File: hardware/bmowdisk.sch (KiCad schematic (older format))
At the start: 22 parts, among them CON1 IDC20, CON2 FL40YA-V36P-2X20-LF, CON3 FL40YA-V36P-2X20-LF, U1 SN74LVC8T245PW, U2 SN74LVC8T245PW, U3 SN74LVC8T245PW, U4 SN74LVC8T245PW

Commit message: Remove silk screen from 0.5" headers
Add text for connections to FPGA board

Signed-off-by: Rangel Ivanov <rangelivanov88@gmail.com>
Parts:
- CON1: value IDC20 -> TO DISK DRIVE
- CON2, CON3: value FL40YA-V36P-2X20-LF -> TO FPGA EXT3 CONN
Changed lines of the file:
@@
-$EndComp
-$Comp
-L bmowdisk-eagle-import:IDC20 CON1
-U 1 1 98085B15
-P 10450 1000
-F 0 "CON1" H 10350 1550 59  0000 L BNN
-F 1 "IDC20" H 10350 300 59  0000 L BNN
-F 2 "bmowdisk:IDC20" H 10450 1000 50  0001 C CNN
-F 3 "" H 10450 1000 50  0001 C CNN
-	1    10450 1000
-	1    0    0    -1
 $EndComp
 $Comp
@@
 	1    9850 500
 	1    0    0    -1
-$EndComp
-$Comp
-L ice40-shield-lib:FL40YA-V36P-2X20-LF CON2
-U 1 1 602FCDEE
-P 2450 2950
-F 0 "CON2" H 2450 1685 50  0000 C CNN
-F 1 "FL40YA-V36P-2X20-LF" H 2450 1776 50  0000 C CNN
-F 2 "lime2-ice40-shield:YA-V36P-2X20-LF" H 2450 1600 50  0000 C CNN
-F 3 "" H 2450 2950 60  0000 C CNN
-	1    2450 2950
-	1    0    0    1
 $EndComp
 Wire Wire Line
@@
 Text Label 2850 5800 0    48   ~ 0
 SEL
-$Comp
-L ice40-shield-lib:FL40YA-V36P-2X20-LF CON3
-U 1 1 610F6C3A
-P 2450 5900
-F 0 "CON3" H 2450 4635 50  0000 C CNN
-F 1 "FL40YA-V36P-2X20-LF" H 2450 4726 50  0000 C CNN
-F 2 "lime2-ice40-shield:YA-V36P-2X20-LF" H 2500 4500 50  0000 C CNN
-F 3 "" H 2450 5900 60  0000 C CNN
-	1    2450 5900
-	1    0    0    1
-$EndComp
 Text Label 2850 5900 0    48   ~ 0
 ~ENABLE1
@@
 NoConn ~ 2800 5100
 NoConn ~ 2800 5200
+$Comp
+L bmowdisk-eagle-import:IDC20 CON1
+U 1 1 98085B15
+P 10450 1000
+F 0 "CON1" H 10350 1550 59  0000 L BNN
+F 1 "TO DISK DRIVE" H 10200 300 59  0000 L BNN
+F 2 "bmowdisk:IDC20" H 10450 1000 50  0001 C CNN
+F 3 "" H 10450 1000 50  0001 C CNN
+	1    10450 1000
+	1    0    0    -1
+$EndComp
+$Comp
+L ice40-shield-lib:FL40YA-V36P-2X20-LF CON3
+U 1 1 610F6C3A
+P 2450 5900
+F 0 "CON3" H 2450 4635 50  0000 C CNN
+F 1 "TO FPGA EXT3 CONN" H 2450 4726 50  0000 C CNN
+F 2 "lime2-ice40-shield:YA-V36P-2X20-LF" H 2500 4500 50  0000 C CNN
+F 3 "" H 2450 5900 60  0000 C CNN
+	1    2450 5900
+	1    0    0    1
+$EndComp
+$Comp
+L ice40-shield-lib:FL40YA-V36P-2X20-LF CON2
+U 1 1 602FCDEE
+P 2450 2950
+F 0 "CON2" H 2450 1685 50  0000 C CNN
+F 1 "TO FPGA EXT3 CONN" H 2450 1776 50  0000 C CNN
+F 2 "lime2-ice40-shield:YA-V36P-2X20-LF" H 2450 1600 50  0000 C CNN
+F 3 "" H 2450 2950 60  0000 C CNN
+	1    2450 2950
+	1    0    0    1
+$EndComp
 $EndSCHEMATC

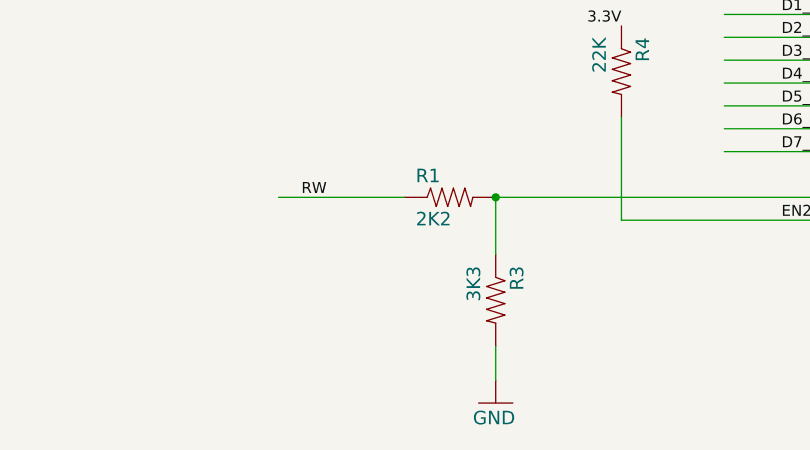
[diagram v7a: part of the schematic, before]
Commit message: Remove voltage divider for RW line to bus transceiver
Signed-off-by: Rangel Ivanov <rangelivanov88@gmail.com>
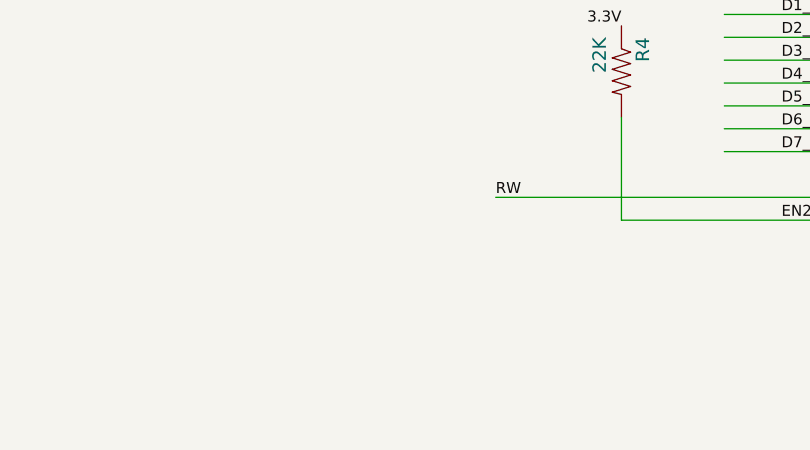
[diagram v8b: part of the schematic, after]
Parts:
- removed R1: 2K2, bmowdisk:R_0805_2012Metric_Pad1.20x1.40mm_HandSolder, symbol bmowdisk-eagle-import:RESISTOR0805-RES
- removed R3: 3K3, bmowdisk:R_0805_2012Metric_Pad1.20x1.40mm_HandSolder, symbol bmowdisk-eagle-import:RESISTOR0805-RES
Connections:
- wire segments 218 -> 215
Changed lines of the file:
@@
 Text Label 6000 9500 0    48   ~ 0
 EN245
-Text Label 3900 9400 0    48   ~ 0
+Text Label 4750 9400 0    48   ~ 0
 RW
-$Comp
-L bmowdisk-eagle-import:RESISTOR0805-RES R1
-U 1 1 62D0D96F
-P 4550 9400
-F 0 "R1" H 4400 9459 59  0000 L BNN
-F 1 "2K2" H 4400 9270 59  0000 L BNN
-F 2 "bmowdisk:R_0805_2012Metric_Pad1.20x1.40mm_HandSolder" H 4550 9400 50  0001 C CNN
-F 3 "" H 4550 9400 50  0001 C CNN
-	1    4550 9400
-	1    0    0    -1
-$EndComp
-$Comp
-L bmowdisk-eagle-import:RESISTOR0805-RES R3
-U 1 1 62D0D975
-P 4750 9850
-F 0 "R3" H 4600 9909 59  0000 L BNN
-F 1 "3K3" H 4600 9720 59  0000 L BNN
-F 2 "bmowdisk:R_0805_2012Metric_Pad1.20x1.40mm_HandSolder" H 4750 9850 50  0001 C CNN
-F 3 "" H 4750 9850 50  0001 C CNN
-	1    4750 9850
-	0    1    1    0
-$EndComp
-Wire Wire Line
-	4750 9400 4750 9650
-Wire Wire Line
-	3800 9400 4350 9400
-Connection ~ 4750 9400
-$Comp
-L bmowdisk-eagle-import:GND #GND0116
-U 1 1 62D0D97F
-P 4750 10300
-F 0 "#GND0116" H 4750 10300 50  0001 C CNN
-F 1 "GND" H 4650 10200 59  0000 L BNN
-F 2 "" H 4750 10300 50  0001 C CNN
-F 3 "" H 4750 10300 50  0001 C CNN
-	1    4750 10300
-	1    0    0    -1
-$EndComp
-Wire Wire Line
-	4750 10050 4750 10200
 Wire Wire Line
 	4750 9400 6500 9400
